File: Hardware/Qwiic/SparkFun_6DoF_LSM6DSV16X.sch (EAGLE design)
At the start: 31 parts, among them J1 QWIIC_RIGHT_ANGLE, J2 QWIIC_RIGHT_ANGLE, U2 LSM6DSV16X

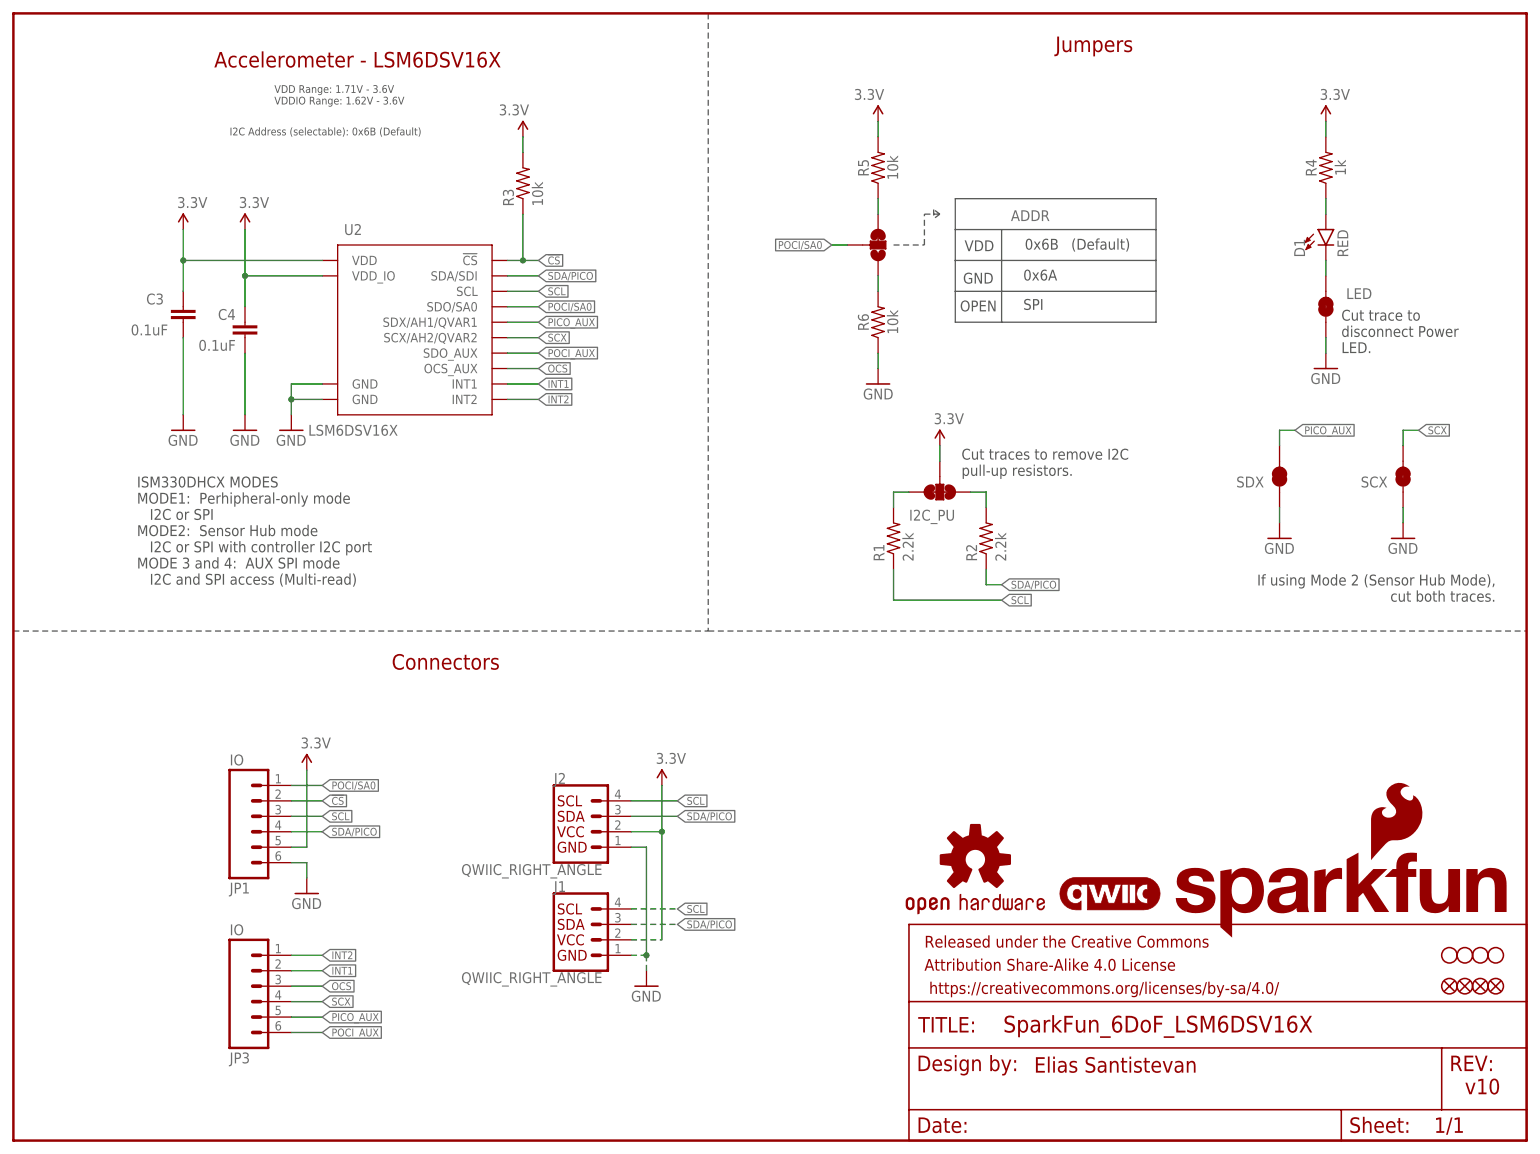
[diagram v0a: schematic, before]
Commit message: Approves air wires, shuffles schematic
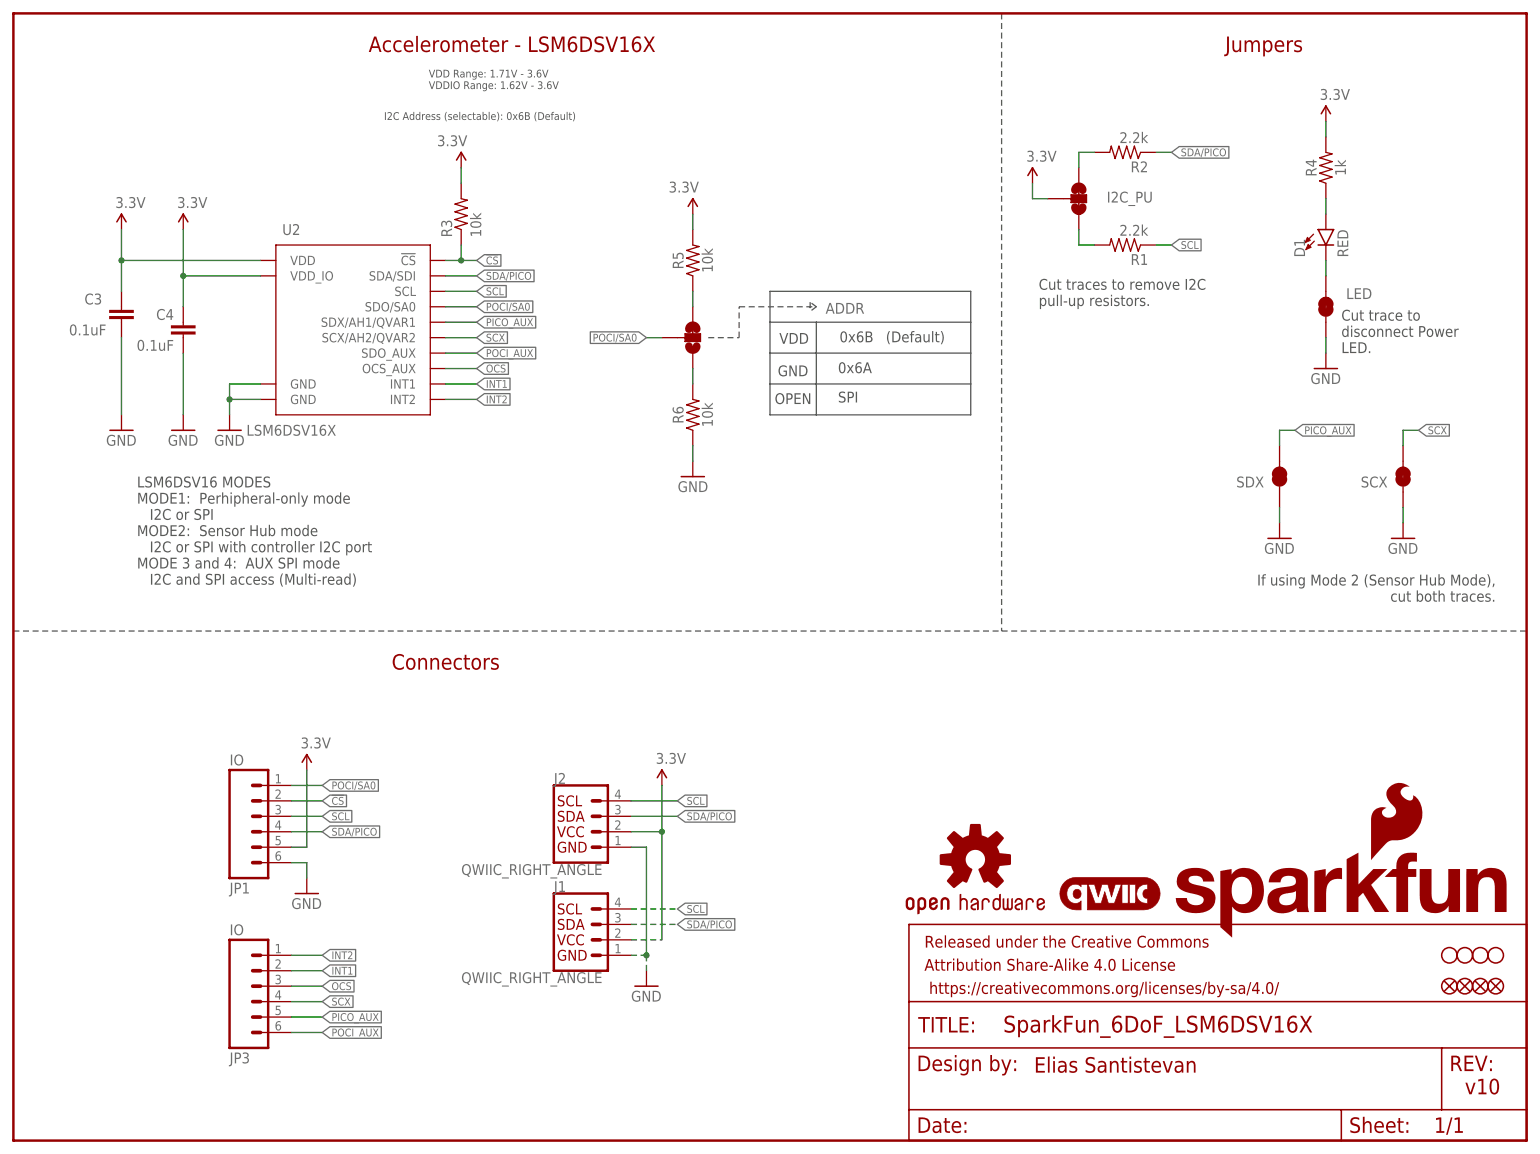
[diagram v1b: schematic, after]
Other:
- note added: "LSM6DSV16 MODES MODE1: Perhipheral-only mode I2C or SPI MODE2: Sensor Hub mode I2C or SPI with controller I2C port MODE 3 and 4: AUX SPI mode I2C and SPI access (Multi-read)"
- note removed: "ISM330DHCX MODES MODE1: Perhipheral-only mode I2C or SPI MODE2: Sensor Hub mode I2C or SPI with controller I2C port MODE 3 and 4: AUX SPI mode I2C and SPI access (Multi-read)"
- moved on the sheet: ADDR, C3, C4, I2C_PU, R1, R2, R3, R5, R6, U2
